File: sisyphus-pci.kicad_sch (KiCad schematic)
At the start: 124 parts, among them J1 Bus_PCI_32bit_Universal, J10 LINE_OUT, J2 JOYSTICK, J3 CD_IN, J4 WAVE_BLASTER, J5 LINE_IN_HDR, J6 LINE_IN_3.5, J7 HEADPHONE_OUT, J8 PCPCI, J9 LINE_OUT_3.5M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

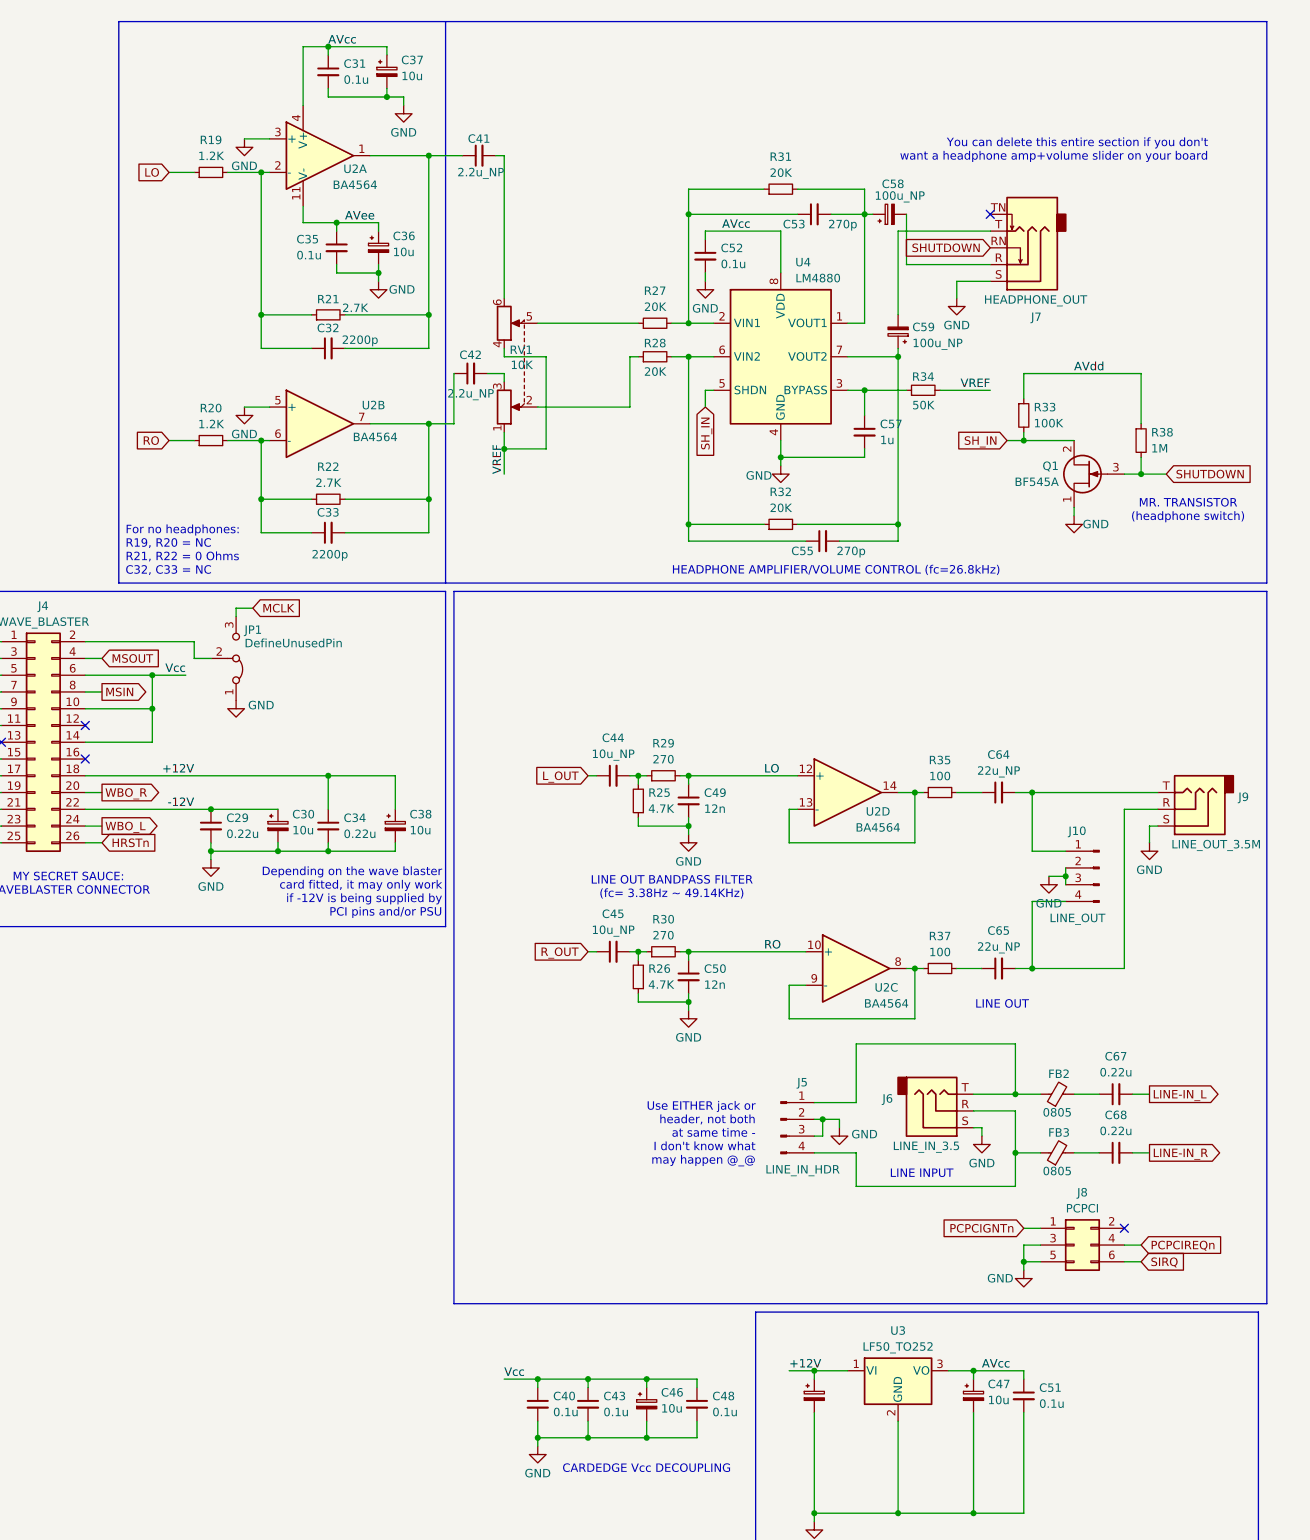
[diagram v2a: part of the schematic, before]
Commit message: Add files via upload
Introducing the LC branch, which is a cost-reduced version with a much smaller board and reduced jacks etc.
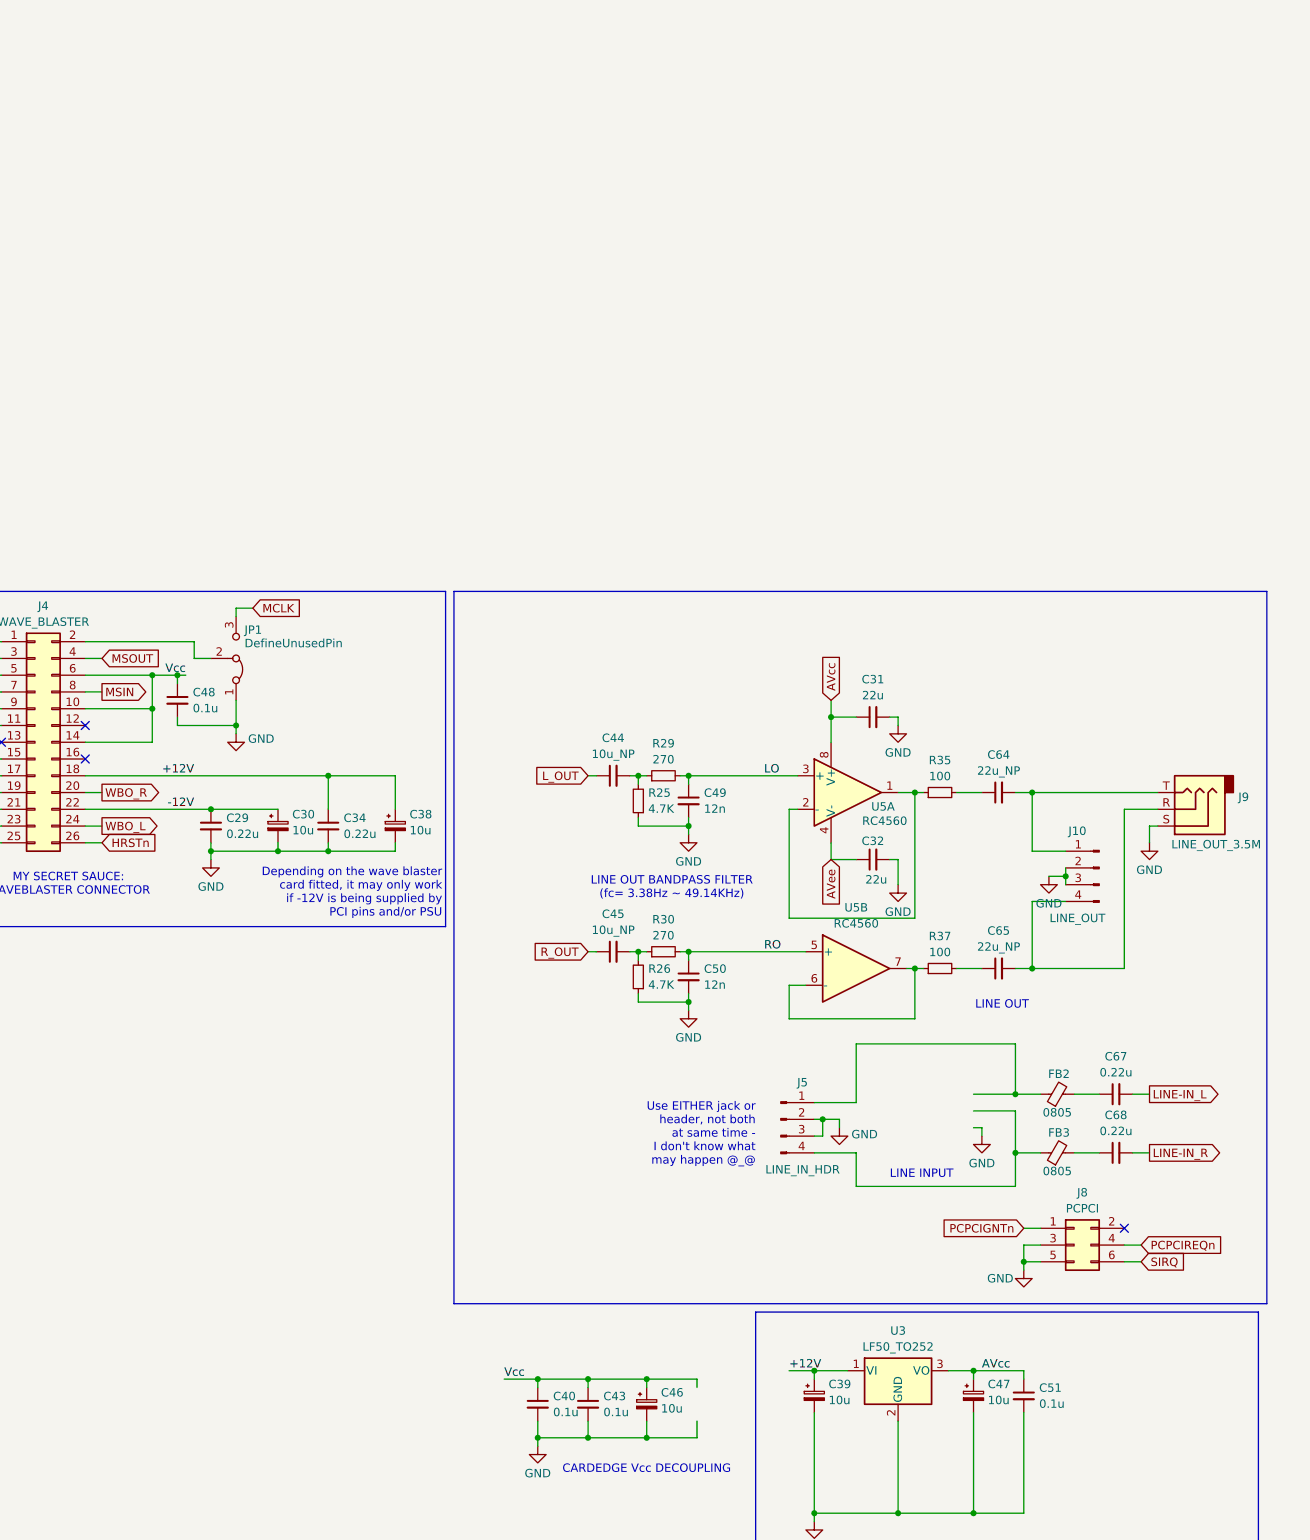
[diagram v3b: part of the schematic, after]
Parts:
- removed C33: 2200p, Capacitor_SMD:C_0805_2012Metric, symbol Device:C_Small
- removed C35, C52: 0.1u, Capacitor_SMD:C_0805_2012Metric, symbol Device:C_Small
- removed C36, C37: 10u, Capacitor_SMD:C_1206_3216Metric, symbol Device:C_Polarized_Small
- removed C41, C42: 2.2u_NP, Capacitor_THT:CP_Radial_D5.0mm_P2.00mm, symbol Device:C_Small
- removed C53, C55: 270p, Capacitor_SMD:C_0805_2012Metric, symbol Device:C_Small
- removed C57: 1u, Capacitor_THT:CP_Radial_D5.0mm_P2.00mm, symbol Device:C_Small
- removed C58, C59: 100u_NP, Capacitor_THT:CP_Radial_D5.0mm_P2.00mm, symbol Device:C_Polarized_Small
- removed J6: LINE_IN_3.5, Connector_Audio:Jack_3.5mm_CUI_SJ1-3523N_Horizontal, symbol Connector_Audio:AudioJack3
- removed J7: HEADPHONE_OUT, Connector_Audio:Jack_3.5mm_CUI_SJ1-3525N_Horizontal, symbol Connector_Audio:AudioJack3_SwitchTR
- removed Q1: BF545A, Package_TO_SOT_SMD:SOT-23, symbol Transistor_FET:BF545A
- removed R19, R20: 1.2K, Resistor_SMD:R_0805_2012Metric, symbol Device:R_Small
- removed R21, R22: 2.7K, Resistor_SMD:R_0805_2012Metric, symbol Device:R_Small
- removed R27, R28, R31, R32: 20K, Resistor_SMD:R_0805_2012Metric, symbol Device:R_Small
- removed R33: 100K, Resistor_SMD:R_0805_2012Metric, symbol Device:R_Small
- removed R34: 50K, Resistor_SMD:R_0805_2012Metric, symbol Device:R_Small
- removed R38: 1M, Resistor_SMD:R_0805_2012Metric, symbol Device:R_Small
- removed RV1: 10K, Potentiometer_THT:Potentiometer_Alps_RK09L_Double_Horizontal, symbol Device:R_Potentiometer_Dual
- removed U2: BA4564, TSSOP_SSOP:TSSOP_SSOP_14, symbol Amplifier_Operational:TL074
- removed U4: LM4880, Package_SO:SOIC-8_3.9x4.9mm_P1.27mm, symbol Amplifier_Audio:LM4810
- added U5: RC4560, SOIC8_DMP8:SOIC-8_DMP-8, symbol Amplifier_Operational:RC4560
- C23: footprint Capacitor_SMD:C_0805_2012Metric -> Capacitor_SMD:C_1206_3216Metric
- C28: footprint Capacitor_THT:CP_Radial_D5.0mm_P2.00mm -> Capacitor_SMD:C_1210_3225Metric
- C30, C38, C46, C56: footprint Capacitor_THT:CP_Radial_D5.0mm_P2.00mm -> Capacitor_SMD:C_1206_3216Metric
- C31: value 0.1u -> 22u; footprint Capacitor_SMD:C_0805_2012Metric -> Capacitor_SMD:C_1206_3216Metric
- C32: value 2200p -> 22u; footprint Capacitor_SMD:C_0805_2012Metric -> Capacitor_SMD:C_1206_3216Metric
- C39, C47, C61: footprint Capacitor_THT:CP_Radial_D5.0mm_P2.00mm -> Capacitor_SMD:CP_Elec_5x5.3
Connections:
- net AVcc: now also U5.8 (V+)
- net AVee: now also C32.1, U5.4 (V-)
- net GND: now also C32.2
- net LO: now also U5.3 (+)
- net RO: now also U5.5 (+)
- net at R37.1: now also U5.6 (-), U5.7
- net at R35.1: now also U5.1, U5.2 (-)
- no-connect marks 43 -> 42
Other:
- note removed: "For no headphones: R19, R20 = NC R21, R22 = 0 Ohms C32, C33 = NC"
- note removed: "HEADPHONE AMPLIFIER/VOLUME CONTROL (fc=26.8kHz)"
- note removed: "MR. TRANSISTOR (headphone switch)"
- note removed: "You can delete this entire section if you don't want a headphone amp+volume slider on your board"
- moved on the sheet: C48
